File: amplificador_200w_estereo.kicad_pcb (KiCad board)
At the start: 2 copper layers, 130 x 105 mm, 108 parts, among them J1 Conn_01x03, J2 input, J4 out, J5 in_aux, Q1 A733, Q10 A733, Q11 A733, Q12 2SC2229, Q13 2SC2229, Q14 BD139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

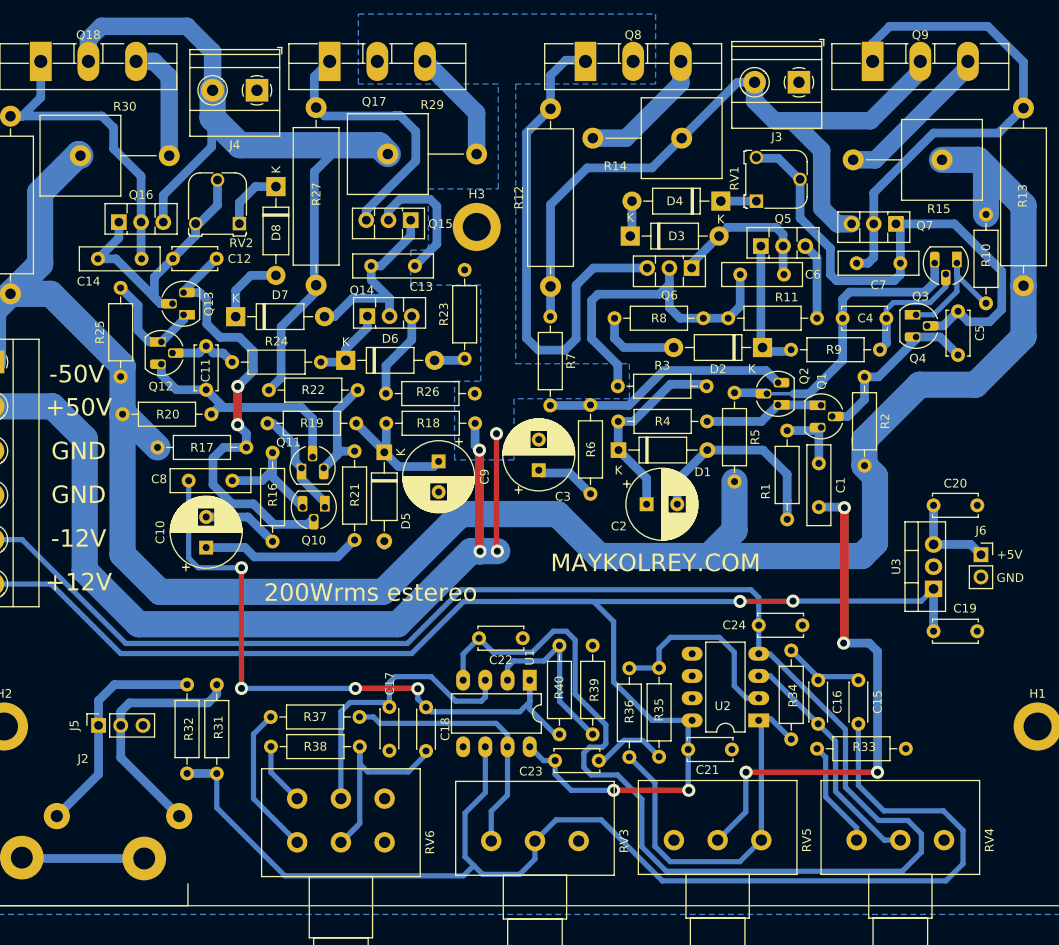
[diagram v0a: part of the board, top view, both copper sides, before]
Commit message: Separando las altas con resistencias de 22K
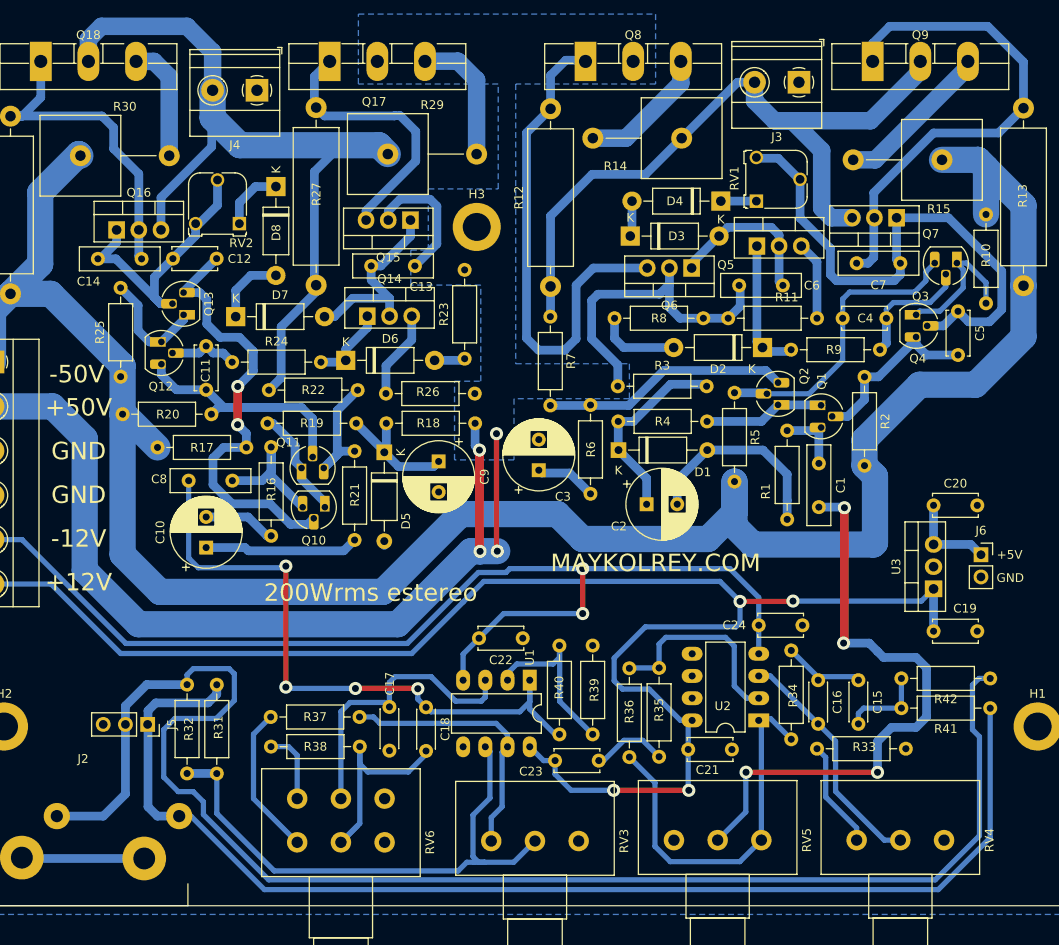
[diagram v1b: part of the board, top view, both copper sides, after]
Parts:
- added R31: 22K, Resistor_THT:R_Axial_DIN0207_L6.3mm_D2.5mm_P10.16mm_Horizontal, F.Cu at (124.3, 84.0)
- added R31: 22K, Resistor_THT:R_Axial_DIN0207_L6.3mm_D2.5mm_P10.16mm_Horizontal, F.Cu at (124.3, 87.4)
- Q14, Q16, Q5, Q7: value BD139 -> TIP42C; footprint Package_TO_SOT_THT:TO-126-3_Vertical -> Package_TO_SOT_THT:TO-220-3_Vertical
- Q15, Q6: value BD136 -> TIP41C; footprint Package_TO_SOT_THT:TO-126-3_Vertical -> Package_TO_SOT_THT:TO-220-3_Vertical
- moved J5 5.62 mm to (27.9, 89.3), turned to -90 degrees
- moved C6 1.25 mm to (100.6, 39.0)
- moved Q16 0.93 mm to (24.3, 32.7)
- moved Q7 0.70 mm to (113.6, 31.3)
- moved R16 0.67 mm to (42.0, 57.5)
- moved Q5 0.45 mm to (97.6, 34.5)
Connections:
- J5 pad 1: /crossover/IN-R -> /crossover/IN-L
- J5 pad 2: /crossover/IN-L -> /crossover/IN-R
- R31 pad 2: /crossover/pasa-altas/IN -> Net-(R31-Pad2)
- R32 pad 2: /crossover/pasa-altas/IN -> Net-(R31-Pad2)
- RV3 pad 2: /crossover/pasa-altas/IN -> Net-(R31-Pad2)
- U1 pad 6: /crossover/pasa-altas/IN -> Net-(R31-Pad2)
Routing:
- net /crossover/IN-R: track 26.1 -> 173.1 mm
- net /crossover/pasa-altas/IN: track 144.2 -> 9.77 mm
- net /crossover/IN-L: track 27.6 -> 138.3 mm
- net -12V: track 219.2 -> 127.6 mm, vias 0 -> 2
- net Net-(R31-Pad2): track 0.00 -> 64.2 mm
- net /channel-a/IN_SIGNAL: track 60.7 -> 69.1 mm
- net +12V: track 177.7 -> 182.1 mm
- net Net-(Q17-Pad3): track 13.1 -> 15.3 mm
- net Net-(Q3-Pad1): track 15.1 -> 16.4 mm
- net Net-(C8-Pad1): track 14.8 -> 16.1 mm
- net 50V: track 162.9 -> 161.7 mm
- net Net-(R38-Pad1): track 7.19 -> 8.37 mm
- net /channel-b/OUT: track 98.1 -> 99.1 mm
- net /channel-a/OUT: track 85.1 -> 84.2 mm
- net Net-(C5-Pad1): track 61.9 -> 62.8 mm
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
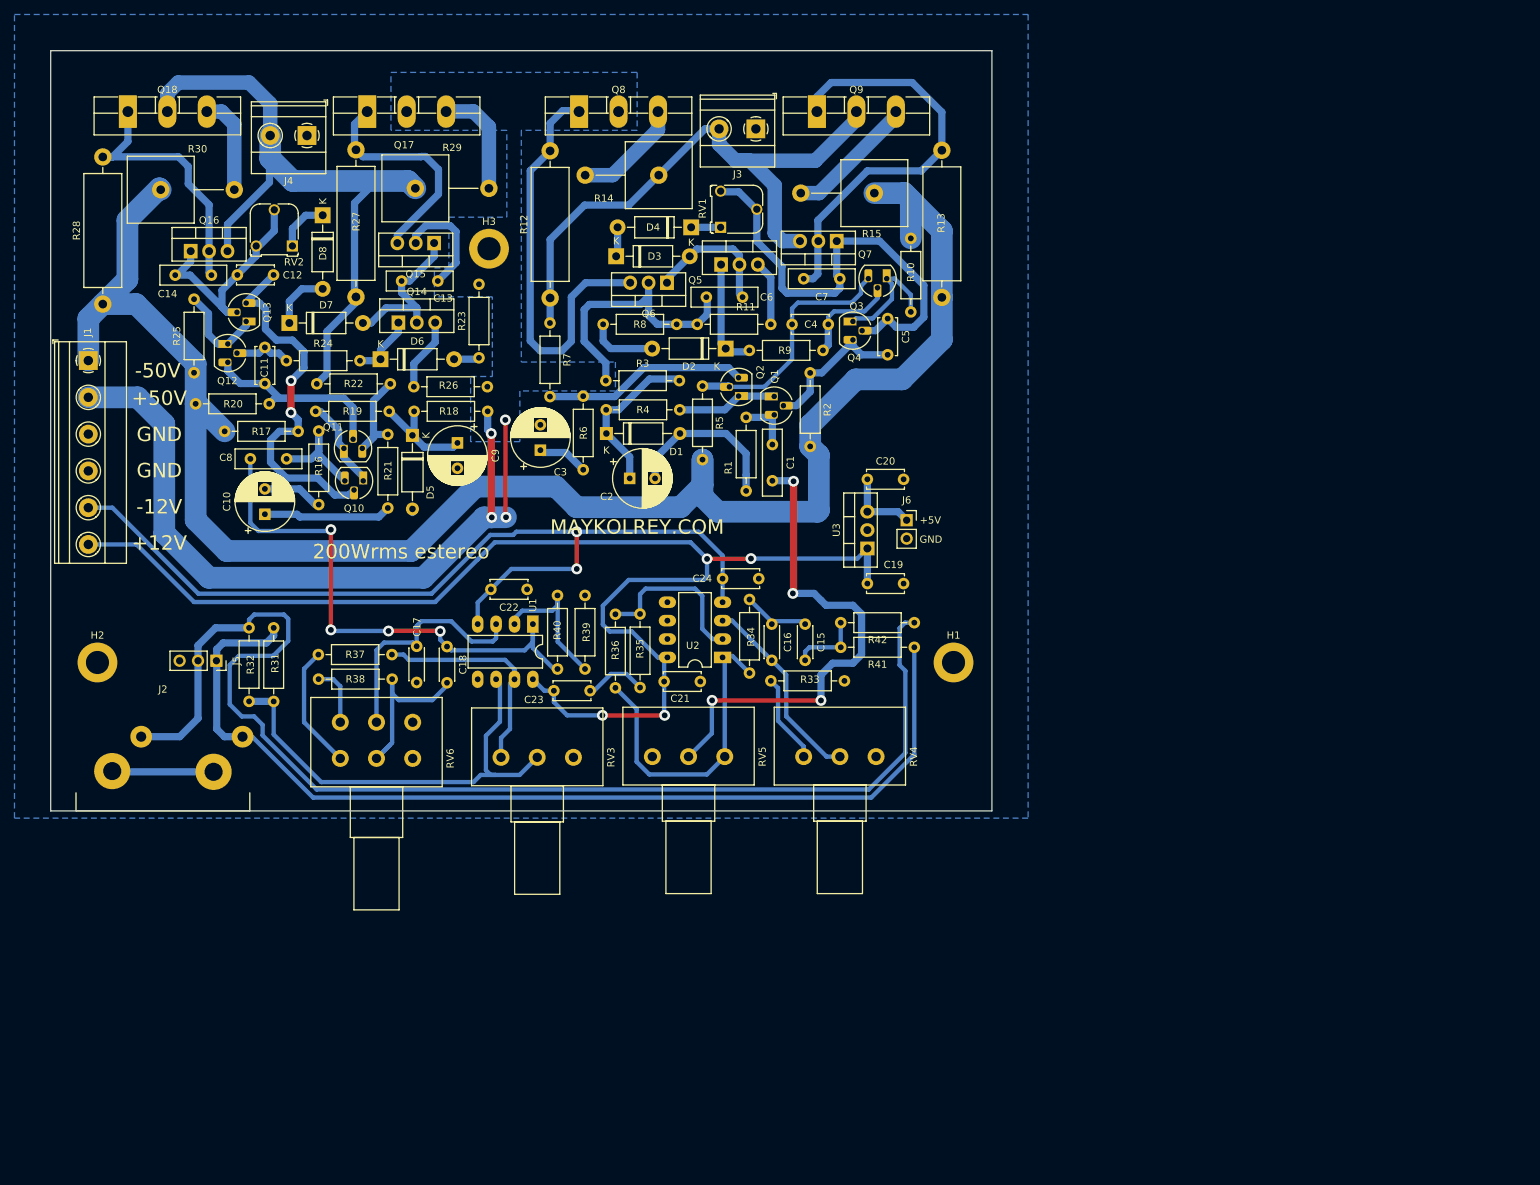
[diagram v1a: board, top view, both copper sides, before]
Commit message: actualizando a kicad 7
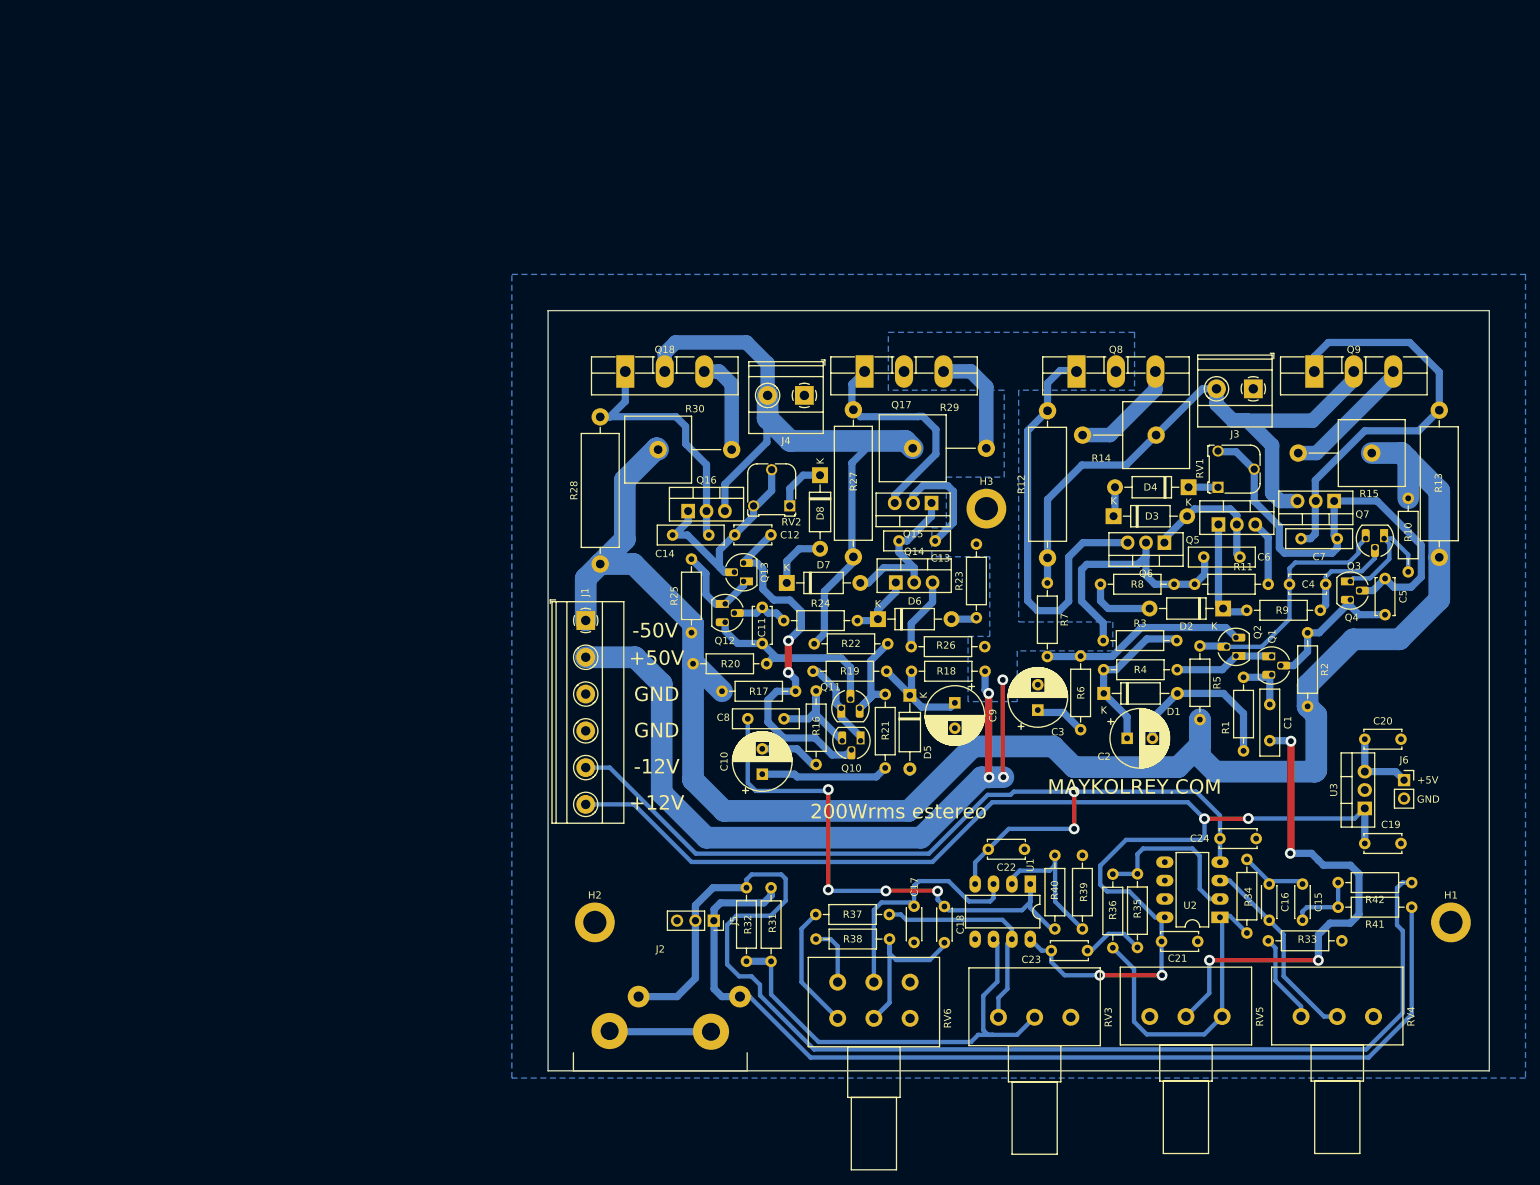
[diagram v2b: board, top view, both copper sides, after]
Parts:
- moved C5 77.5 mm to (189.3, 77.9)
- moved H1 77.5 mm to (198.4, 125.4)
- moved J? 77.5 mm to (191.9, 105.8)
- moved Q2 77.5 mm to (168.7, 88.6)
- moved Q7 77.5 mm to (182.3, 67.2)
- moved RV5 77.5 mm to (156.8, 138.4)
- moved C1 77.5 mm to (173.4, 95.3)
- moved C12 77.5 mm to (99.5, 71.9)
- moved C13 77.5 mm to (122.2, 72.7)
- moved C14 77.5 mm to (90.9, 71.9)
- moved C16 77.5 mm to (173.3, 125.1)
- moved C19 77.5 mm to (186.5, 114.5)
- moved C21 77.5 mm to (158.4, 128.0)
- moved C3 77.5 mm to (141.3, 96.1)
- moved D2 77.5 mm to (166.9, 82.0)
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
